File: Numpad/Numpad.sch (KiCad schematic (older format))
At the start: 85 parts, among them SW1 SW_Push, U1 ATmega32U4-AU, Y1 16MHz

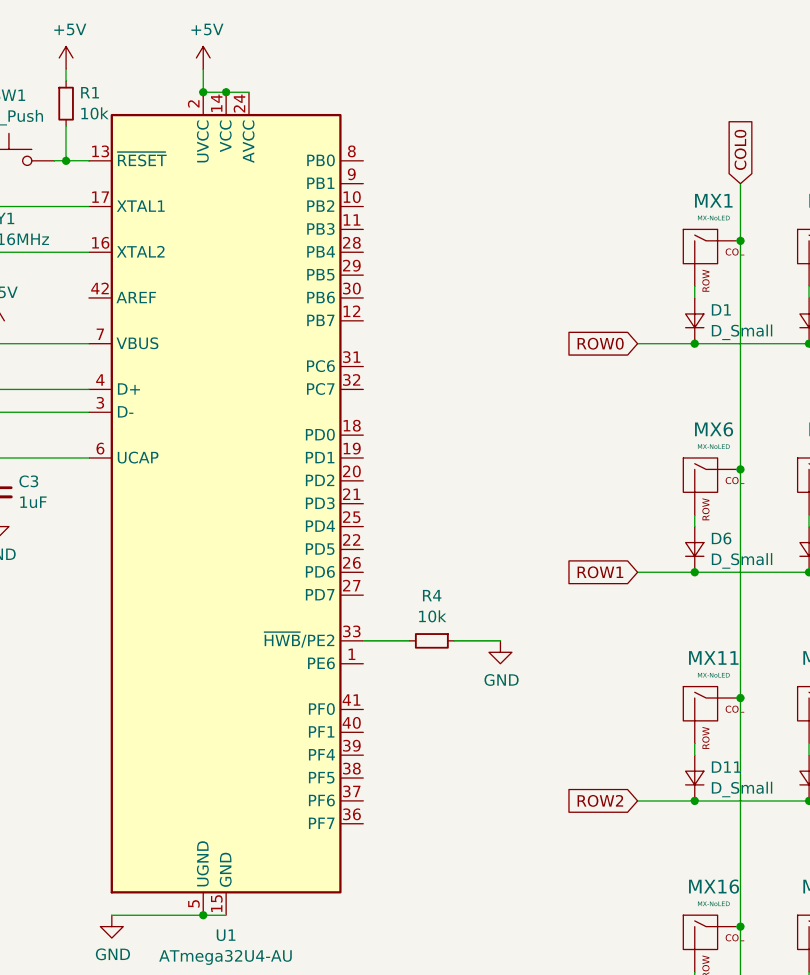
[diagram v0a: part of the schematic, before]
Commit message: finished pcb routing
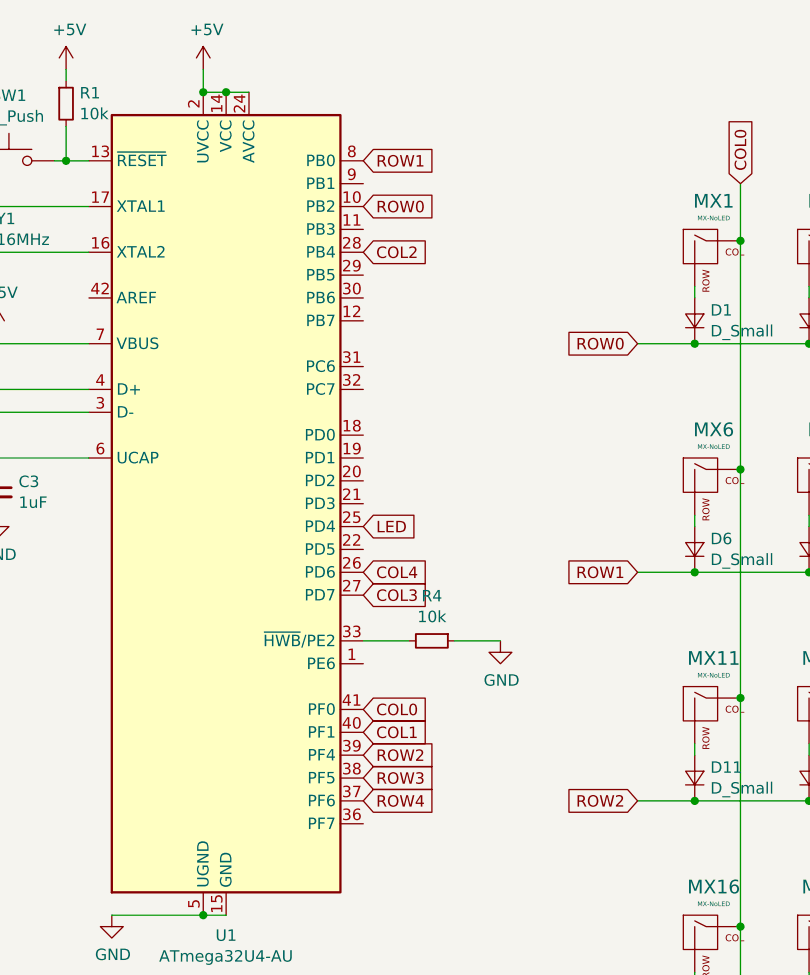
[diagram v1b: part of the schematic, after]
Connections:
- net COL0: now also U1.41 (PF0)
- net COL1: now also U1.40 (PF1)
- net COL2: now also U1.28 (PB4)
- net COL3: now also U1.27 (PD7)
- net COL4: now also U1.26 (PD6)
- net LED: now also U1.25 (PD4)
- net ROW0: now also U1.10 (PB2)
- net ROW1: now also U1.8 (PB0)
- net ROW2: now also U1.39 (PF4)
- net ROW3: now also U1.38 (PF5)
- net ROW4: now also U1.37 (PF6)
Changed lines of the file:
@@
 NoConn ~ 2050 6250
 NoConn ~ 2050 6850
+Text GLabel 3100 1200 2    50   Input ~ 0
+ROW1
+Text GLabel 3100 3600 2    50   Input ~ 0
+COL0
+Text GLabel 3100 3700 2    50   Input ~ 0
+COL1
+Text GLabel 3100 1400 2    50   Input ~ 0
+ROW0
+Text GLabel 3100 1600 2    50   Input ~ 0
+COL2
+Text GLabel 3100 3100 2    50   Input ~ 0
+COL3
+Text GLabel 3100 3000 2    50   Input ~ 0
+COL4
+Text GLabel 3100 3800 2    50   Input ~ 0
+ROW2
+Text GLabel 3100 3900 2    50   Input ~ 0
+ROW3
+Text GLabel 3100 4000 2    50   Input ~ 0
+ROW4
+Text GLabel 3100 2800 2    50   Input ~ 0
+LED
 $EndSCHEMATC
